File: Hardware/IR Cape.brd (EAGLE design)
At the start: 71.8 x 54.6 mm, 32 parts, among them T3 MPSA13RLRAG, T4 MPSA13RLRAG, T5 MPSA13RLRAG, X1 KLBR2, X2 KLBR2, X3 KLBR2

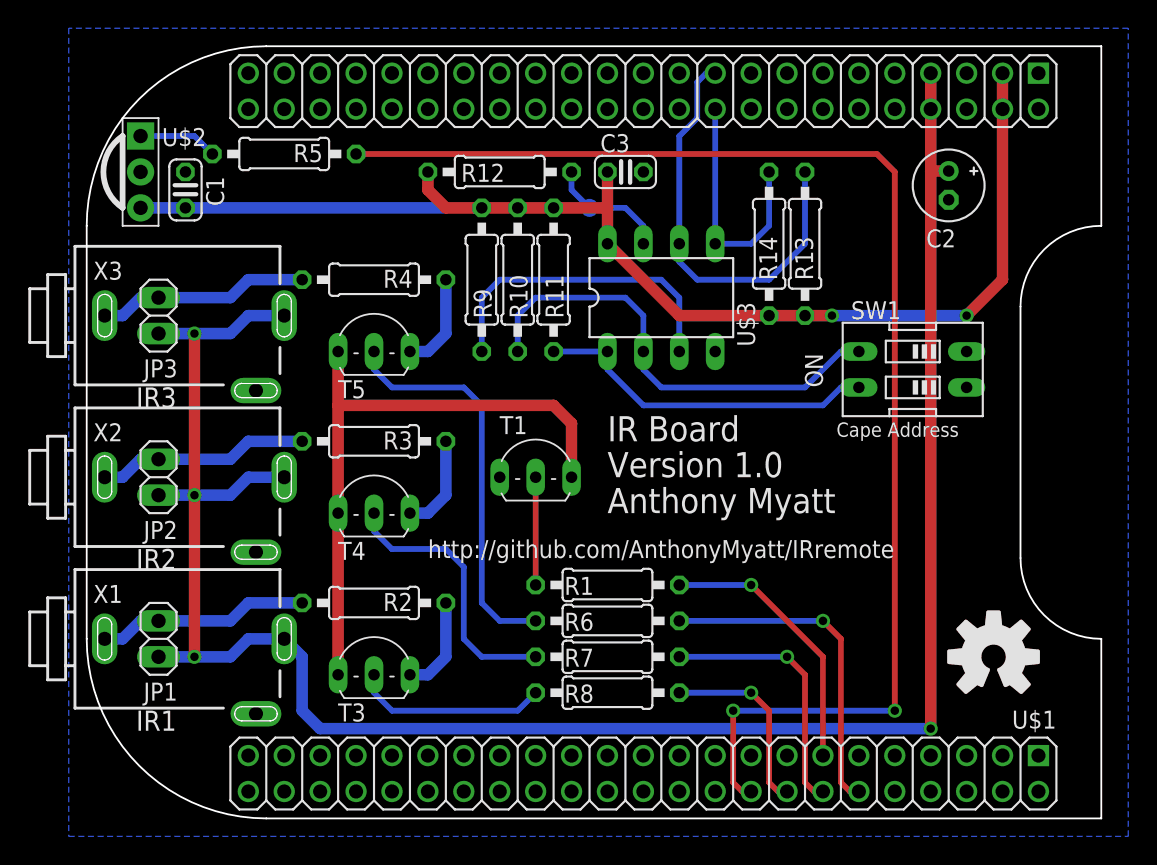
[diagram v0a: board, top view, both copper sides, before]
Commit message: Fixed resistor values in schematic
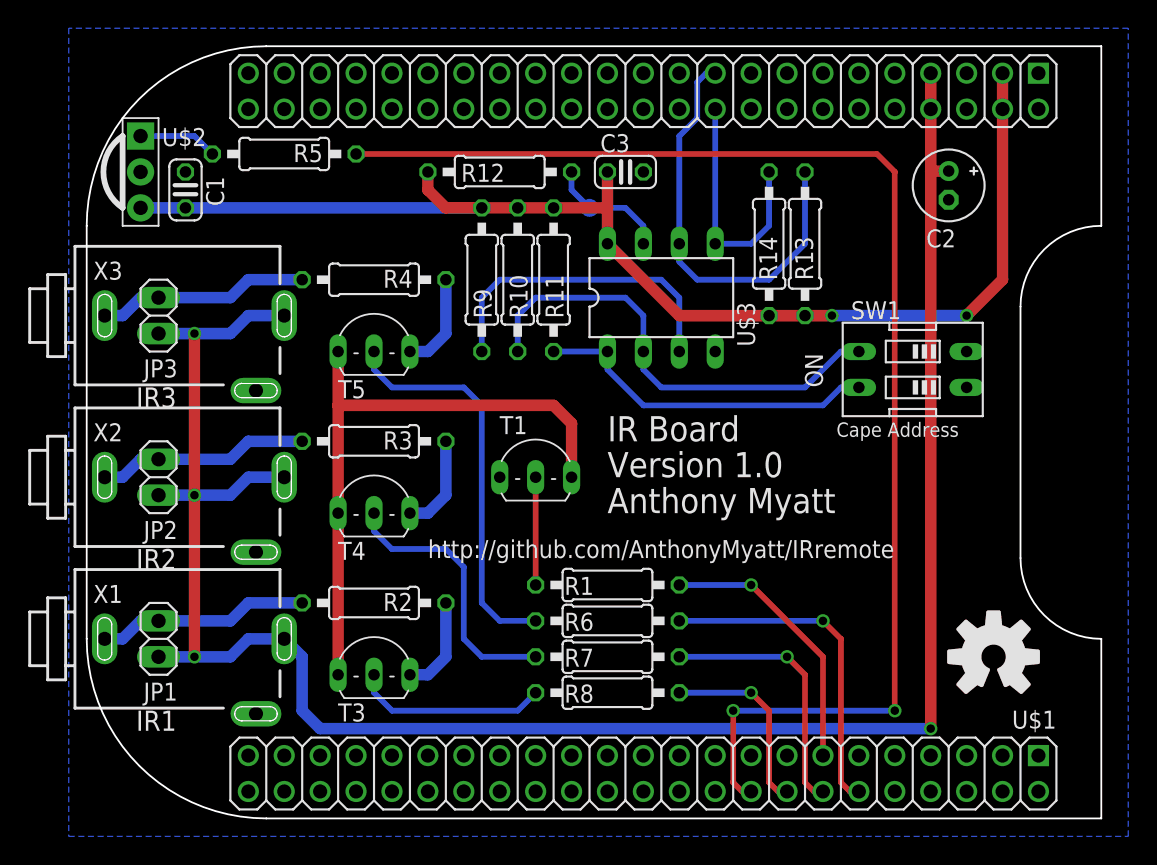
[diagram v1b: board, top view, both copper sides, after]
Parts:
- R1, R6, R7, R8: value 220 -> 1k9
- R2, R3, R4: value 33 -> 10
- T1: value (none) -> MPSA13RLRAG
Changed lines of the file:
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@@
 <layer number="25" name="tNames" color="7" fill="1" visible="yes" active="yes"/>
 <layer number="26" name="bNames" color="7" fill="1" visible="yes" active="yes"/>
-<layer number="27" name="tValues" color="7" fill="1" visible="no" active="yes"/>
-<layer number="28" name="bValues" color="7" fill="1" visible="no" active="yes"/>
-<layer number="29" name="tStop" color="7" fill="3" visible="no" active="yes"/>
-<layer number="30" name="bStop" color="7" fill="6" visible="no" active="yes"/>
+<layer number="27" name="tValues" color="7" fill="1" visible="yes" active="yes"/>
+<layer number="28" name="bValues" color="7" fill="1" visible="yes" active="yes"/>
+<layer number="29" name="tStop" color="7" fill="3" visible="yes" active="yes"/>
+<layer number="30" name="bStop" color="7" fill="6" visible="yes" active="yes"/>
 <layer number="31" name="tCream" color="7" fill="4" visible="no" active="yes"/>
 <layer number="32" name="bCream" color="7" fill="5" visible="no" active="yes"/>
@@
 </class>
 </classes>
-<designrules name="default *">
+<designrules name="OSHPark *">
 <description language="de">&lt;b&gt;EAGLE Design Rules&lt;/b&gt;
 &lt;p&gt;
@@
 Einstellungen hier und speichern die Design Rules unter
 einem neuen Namen ab.</description>
-<description language="en">&lt;b&gt;EAGLE Design Rules&lt;/b&gt;
+<description language="en">&lt;b&gt;Laen's PCB Order Design Rules&lt;/b&gt;
 &lt;p&gt;
-The default Design Rules have been set to cover
-a wide range of applications. Your particular design
-may have different requirements, so please make the
-necessary adjustments and save your customized
-design rules under a new name.</description>
+Please make sure your boards conform to these design rules.</description>
 <param name="layerSetup" value="(1*16)"/>
-<param name="mtCopper" value="0.035mm 0.035mm 0.035mm 0.035mm 0.035mm 0.035mm 0.035mm 0.035mm 0.035mm 0.035mm 0.035mm 0.035mm 0.035mm 0.035mm 0.035mm 0.035mm"/>
-<param name="mtIsolate" value="1.5mm 0.15mm 0.2mm 0.15mm 0.2mm 0.15mm 0.2mm 0.15mm 0.2mm 0.15mm 0.2mm 0.15mm 0.2mm 0.15mm 0.2mm"/>
-<param name="mdWireWire" value="8mil"/>
-<param name="mdWirePad" value="8mil"/>
-<param name="mdWireVia" value="8mil"/>
-<param name="mdPadPad" value="8mil"/>
-<param name="mdPadVia" value="8mil"/>
-<param name="mdViaVia" value="8mil"/>
-<param name="mdSmdPad" value="8mil"/>
-<param name="mdSmdVia" value="8mil"/>
-<param name="mdSmdSmd" value="8mil"/>
+<param name="mtCopper" value="0.0356mm 0.0356mm 0.0356mm 0.0356mm 0.0356mm 0.0356mm 0.0356mm 0.0356mm 0.0356mm 0.0356mm 0.0356mm 0.0356mm 0.0356mm 0.0356mm 0.0356mm 0.0356mm"/>
+<param name="mtIsolate" value="1.5011mm 0.1499mm 0.2007mm 0.1499mm 0.2007mm 0.1499mm 0.2007mm 0.1499mm 0.2007mm 0.1499mm 0.2007mm 0.1499mm 0.2007mm 0.1499mm 0.2007mm"/>
+<param name="mdWireWire" value="6mil"/>
+<param name="mdWirePad" value="6mil"/>
+<param name="mdWireVia" value="6mil"/>
+<param name="mdPadPad" value="6mil"/>
+<param name="mdPadVia" value="6mil"/>
+<param name="mdViaVia" value="6mil"/>
+<param name="mdSmdPad" value="6mil"/>
+<param name="mdSmdVia" value="6mil"/>
+<param name="mdSmdSmd" value="6mil"/>
 <param name="mdViaViaSameLayer" value="8mil"/>
 <param name="mnLayersViaInSmd" value="2"/>
-<param name="mdCopperDimension" value="40mil"/>
-<param name="mdDrill" value="8mil"/>
+<param name="mdCopperDimension" value="15mil"/>
+<param name="mdDrill" value="6mil"/>
 <param name="mdSmdStop" value="0mil"/>
-<param name="msWidth" value="10mil"/>
-<param name="msDrill" value="24mil"/>
-<param name="msMicroVia" value="9.99mm"/>
+<param name="msWidth" value="6mil"/>
+<param name="msDrill" value="13mil"/>
+<param name="msMicroVia" value="13mil"/>
 <param name="msBlindViaRatio" value="0.5"/>
 <param name="rvPadTop" value="0.25"/>
@@
 <param name="rvMicroViaOuter" value="0.25"/>
 <param name="rvMicroViaInner" value="0.25"/>
-<param name="rlMinPadTop" value="10mil"/>
+<param name="rlMinPadTop" value="7mil"/>
 <param name="rlMaxPadTop" value="20mil"/>
-<param name="rlMinPadInner" value="10mil"/>
+<param name="rlMinPadInner" value="7mil"/>
 <param name="rlMaxPadInner" value="20mil"/>
-<param name="rlMinPadBottom" value="10mil"/>
+<param name="rlMinPadBottom" value="7mil"/>
 <param name="rlMaxPadBottom" value="20mil"/>
-<param name="rlMinViaOuter" value="8mil"/>
+<param name="rlMinViaOuter" value="7mil"/>
 <param name="rlMaxViaOuter" value="20mil"/>
-<param name="rlMinViaInner" value="8mil"/>
+<param name="rlMinViaInner" value="7mil"/>
 <param name="rlMaxViaInner" value="20mil"/>
 <param name="rlMinMicroViaOuter" value="4mil"/>
@@
 </autorouter>
 <elements>
-<element name="T1" library="transistor-neu-to92" package="TO92-EBC" value="" x="31.75" y="25.4"/>
-<element name="R1" library="resistor" package="0207/10" value="220" x="36.83" y="16.51" smashed="yes" rot="R180">
+<element name="T1" library="transistor-neu-to92" package="TO92-EBC" value="MPSA13RLRAG" x="31.75" y="25.4" smashed="yes">
+<attribute name="NAME" x="29.21" y="27.178" size="1.27" layer="25" ratio="10"/>
+</element>
+<element name="R1" library="resistor" package="0207/10" value="1k9" x="36.83" y="16.51" smashed="yes" rot="R180">
 <attribute name="NAME" x="33.782" y="15.8115" size="1.27" layer="25" ratio="10"/>
 </element>
 <element name="U$1" library="adafruit" package="BEAGLEBONE_SHIELD" value="" x="86.36" y="0" rot="R90"/>
-<element name="R2" library="resistor" package="0207/10" value="33" x="20.32" y="15.24" smashed="yes" rot="R180">
+<element name="R2" library="resistor" package="0207/10" value="10" x="20.32" y="15.24" smashed="yes" rot="R180">
 <attribute name="NAME" x="23.0505" y="15.9385" size="1.27" layer="25" ratio="10" rot="R180"/>
 </element>
-<element name="R3" library="resistor" package="0207/10" value="33" x="20.32" y="26.67" smashed="yes" rot="R180">
+<element name="R3" library="resistor" package="0207/10" value="10" x="20.32" y="26.67" smashed="yes" rot="R180">
 <attribute name="NAME" x="23.0505" y="27.3685" size="1.27" layer="25" ratio="10" rot="R180"/>
 </element>
-<element name="R4" library="resistor" package="0207/10" value="33" x="20.32" y="38.1" smashed="yes" rot="R180">
+<element name="R4" library="resistor" package="0207/10" value="10" x="20.32" y="38.1" smashed="yes" rot="R180">
 <attribute name="NAME" x="23.0505" y="38.7985" size="1.27" layer="25" ratio="10" rot="R180"/>
 </element>
@@
 <attribute name="NAME" x="9.7155" y="43.307" size="1.27" layer="25" ratio="10" rot="R90"/>
 </element>
-<element name="R6" library="resistor" package="0207/10" value="220" x="36.83" y="13.97" smashed="yes">
+<element name="R6" library="resistor" package="0207/10" value="1k9" x="36.83" y="13.97" smashed="yes">
 <attribute name="NAME" x="33.782" y="13.2715" size="1.27" layer="25" ratio="10"/>
 </element>
-<element name="R7" library="resistor" package="0207/10" value="220" x="36.83" y="11.43" smashed="yes">
+<element name="R7" library="resistor" package="0207/10" value="1k9" x="36.83" y="11.43" smashed="yes">
 <attribute name="NAME" x="33.782" y="10.7315" size="1.27" layer="25" ratio="10"/>
 </element>
-<element name="R8" library="resistor" package="0207/10" value="220" x="36.83" y="8.89" smashed="yes">
+<element name="R8" library="resistor" package="0207/10" value="1k9" x="36.83" y="8.89" smashed="yes">
 <attribute name="NAME" x="33.782" y="8.1915" size="1.27" layer="25" ratio="10"/>
 </element>
